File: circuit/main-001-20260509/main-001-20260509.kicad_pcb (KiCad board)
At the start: 2 copper layers, 43.3 x 83.2 mm, 20 parts, among them J1 Conn_Relay, J2 Conn_Sub, Q1 BSS138, Q2 BSS138, SW1 RESET, U1 DEV-16771, U2 BNO055

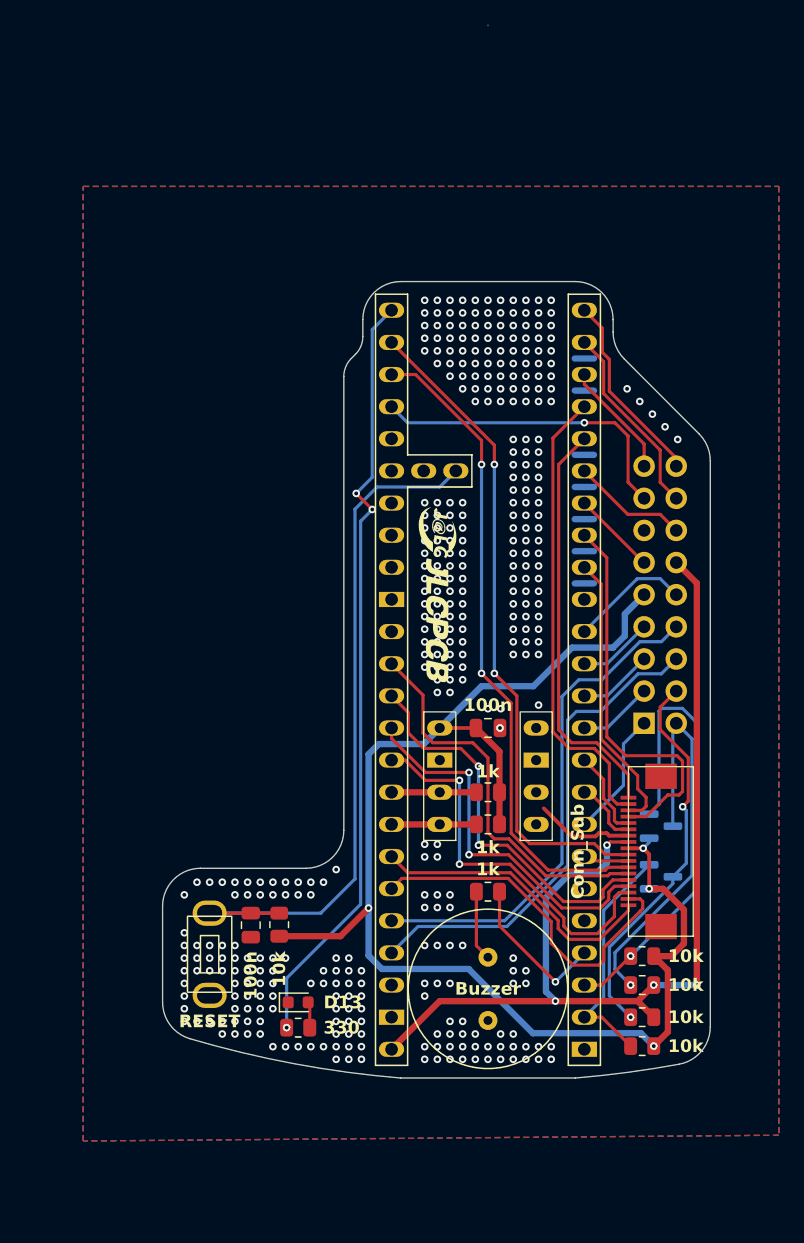
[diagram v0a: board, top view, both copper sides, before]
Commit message: Update メイン基板に使用するFPCコネクタを変更・修正
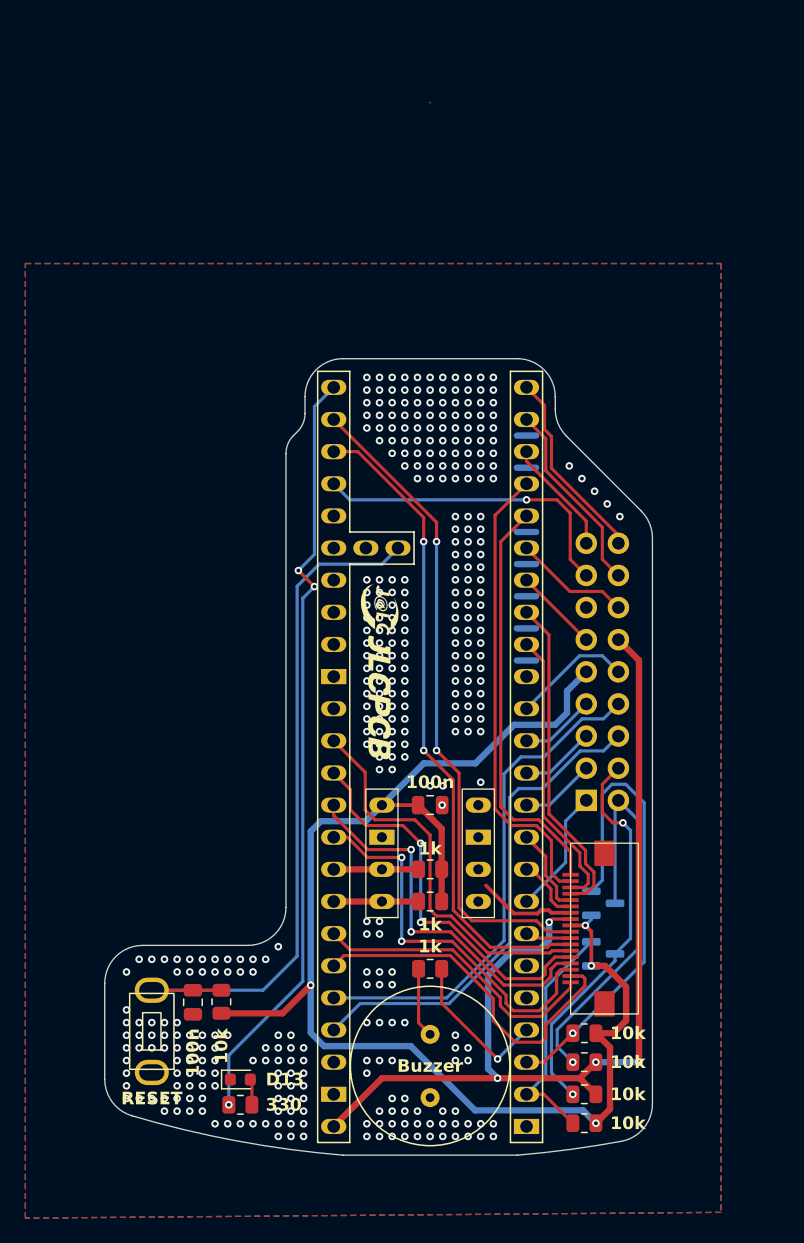
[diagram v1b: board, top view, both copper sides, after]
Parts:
- J2: footprint @Thrive_footprint_main:FPC-05F-18PH20 -> @Thrive_footprint_main:AFC01-S18FCA-00
- moved J2 7.74 mm to (108.7, 119.2)
- moved R4 7.62 mm to (107.4, 129.8)
- moved C1 7.62 mm to (95.2, 109.5)
- moved C2 7.62 mm to (76.5, 125.1)
- moved J1 7.62 mm to (107.6, 109.1)
- moved R1 7.62 mm to (107.4, 134.6)
- moved R3 7.62 mm to (107.4, 132.3)
- moved R5 7.62 mm to (95.2, 114.6)
- moved R6 7.62 mm to (95.2, 122.4)
- moved R8 7.62 mm to (78.8, 125.0)
- moved U1 7.62 mm to (95.2, 105.7)
- moved U2 7.62 mm to (95.2, 113.3)
- moved BZ1 7.62 mm to (95.2, 130.1)
- moved D1 7.62 mm to (80.2, 131.2)
- moved R2 7.62 mm to (107.4, 127.5)
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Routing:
- net RX_{teensy}-TX_{unitV3}: track 31.0 -> 26.0 mm
